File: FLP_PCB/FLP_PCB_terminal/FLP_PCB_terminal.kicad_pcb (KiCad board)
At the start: 2 copper layers, 84.1 x 84.1 mm, 79 parts, among them J1 SMA-J-P-X-ST-TH1, J2 OLED, Q1 Q_PMOS_DSG, U1 AMS1117-3.3, U2 STM32F103C8T6, U3 L86-M33, U4 MCP73831-2-OT, U5 CP2104, U6 TPS61200DRC, U7 USBLC6-2P6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

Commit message: PCB
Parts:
- Y2: footprint Crystal:Crystal_SMD_2012-2Pin_2.0x1.2mm -> Crystal:Crystal_SMD_2016-4Pin_2.0x1.6mm
- moved S2 178.8 mm to (49.0, 129.3)
- moved S1 178.8 mm to (49.0, 124.5)
- moved R3 168.1 mm to (71.5, 154.5)
- moved R4 149.6 mm to (71.5, 152.9)
- moved R8 148.1 mm to (94.7, 154.4)
- moved R16 146.3 mm to (94.7, 155.5)
- moved R9 146.1 mm to (94.7, 153.1)
- moved R17 145.9 mm to (94.7, 156.7)
- moved U7 140.1 mm to (111.0, 154.4), turned to 180 degrees
- moved C28 137.8 mm to (60.0, 134.3)
- moved R1 132.4 mm to (57.4, 123.7), turned to 180 degrees
- moved R2 132.1 mm to (57.4, 125.5), turned to 180 degrees
- moved C17 128.5 mm to (94.7, 149.4), turned to 180 degrees
- moved C18 125.3 mm to (94.7, 147.8)
- moved UART1 121.8 mm to (120.0, 154.2), turned to 90 degrees
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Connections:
- D1 pad A: (no net) -> 5v OUT
- D1 pad C: (no net) -> Net-(Charger1-VBUS)
- U2 pad 1: 3.3V OUT -> unconnected-(U2-VBAT-Pad1)
- U2 pad 18: PB0 -> unconnected-(U2-PB0-Pad18)
- Y2 pad 1: Net-(U8-XTB) -> (no net)
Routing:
- net Net-(BT1-+): track 0.00 -> 78.3 mm, vias 0 -> 2
- net 5v OUT: track 0.00 -> 74.0 mm, vias 0 -> 4
- net BOOT0: track 0.00 -> 70.7 mm, vias 0 -> 2
- net I2C SCL: track 0.00 -> 66.1 mm
- net I2C SDL: track 0.00 -> 54.2 mm, vias 0 -> 2
- net NRST: track 0.00 -> 48.7 mm, vias 0 -> 2
- net 3.3V OUT: track 116.4 -> 68.3 mm, vias 8 -> 29
- net Buzzer: track 0.00 -> 43.2 mm, vias 0 -> 6
- net Net-(Charger1-VBUS): track 0.00 -> 43.1 mm, vias 0 -> 2
- net Find_Host: track 0.00 -> 43.0 mm, vias 0 -> 2
- net ID: track 0.00 -> 40.0 mm, vias 0 -> 2
- net Net-(U5-REGIN): track 0.00 -> 36.0 mm, vias 0 -> 3
- net Net-(Q1-D): track 0.00 -> 34.6 mm, vias 0 -> 2
- net Net-(U6-UVLO): track 0.00 -> 29.3 mm, vias 0 -> 4
- net PC_OSC_IN: track 0.00 -> 28.3 mm
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- added copper zone on In1.Cu, net 3.3V OUT
- added copper zone on B.Cu, net GND
- added copper zone on F.Cu, net GND
- added copper zone on In2.Cu, net GND
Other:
- board size 84.1 x 84.1 mm -> 80 x 80 mm
- copper layers 2 -> 4

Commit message: PCB finish
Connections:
- UART1 pad A1_B12: (no net) -> GND
- UART1 pad B1_A12: (no net) -> GND
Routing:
- net GND: track 149.5 -> 157.4 mm, vias 58 -> 60
- net Net-(U5-REGIN): track 36.0 -> 38.2 mm

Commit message: code adding
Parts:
- BZ1: footprint Buzzer_Beeper:Buzzer_15x7.5RM7.6 -> Buzzer_Beeper:Buzzer_12x9.5RM7.6
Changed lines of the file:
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@@
 			(outputformat 1)
 			(mirror no)
-			(drillshape 1)
+			(drillshape 0)
 			(scaleselection 1)
 			(outputdirectory "")
@@
 		)
 	)
-	(footprint "Buzzer_Beeper:Buzzer_15x7.5RM7.6"
+	(footprint "Buzzer_Beeper:Buzzer_12x9.5RM7.6"
 		(layer "F.Cu")
 		(at 71.28 118.25)
-		(descr "Generic Buzzer, D15mm height 7.5mm with RM7.6mm")
+		(descr "Generic Buzzer, D12mm height 9.5mm with RM7.6mm")
 		(tags "buzzer")
 		(property "Reference" "BZ1"
-			(at 13.13 0.24 0)
+			(at 3.8 -7.2 0)
 			(layer "F.SilkS")
 			(effects
@@
 		)
 		(property "Value" "Buzzer"
-			(at 3.81 8.89 0)
+			(at 3.8 7.4 0)
 			(layer "F.Fab")
 			(effects
@@
 			)
 		)
-		(property "Description" "Buzzer, polarized"
+		(property "Description" ""
 			(at 0 0 0)
 			(unlocked yes)
@@
 		(fp_circle
 			(center 3.8 0)
-			(end 11.4 0)
+			(end 9.9 0)
 			(stroke
 				(width 0.12)
@@
 		(fp_circle
 			(center 3.8 0)
-			(end 11.55 0)
+			(end 10.05 0)
 			(stroke
 				(width 0.05)
@@
 		(fp_circle
 			(center 3.8 0)
-			(end 11.3 0)
+			(end 9.8 0)
 			(stroke
 				(width 0.1)
@@
 		)
 		(embedded_fonts no)
-		(model "${KICAD9_3DMODEL_DIR}/Buzzer_Beeper.3dshapes/Buzzer_15x7.5RM7.6.wrl"
+		(model "${KICAD9_3DMODEL_DIR}/Buzzer_Beeper.3dshapes/Buzzer_12x9.5RM7.6.wrl"
 			(offset
 				(xyz 0 0 0)

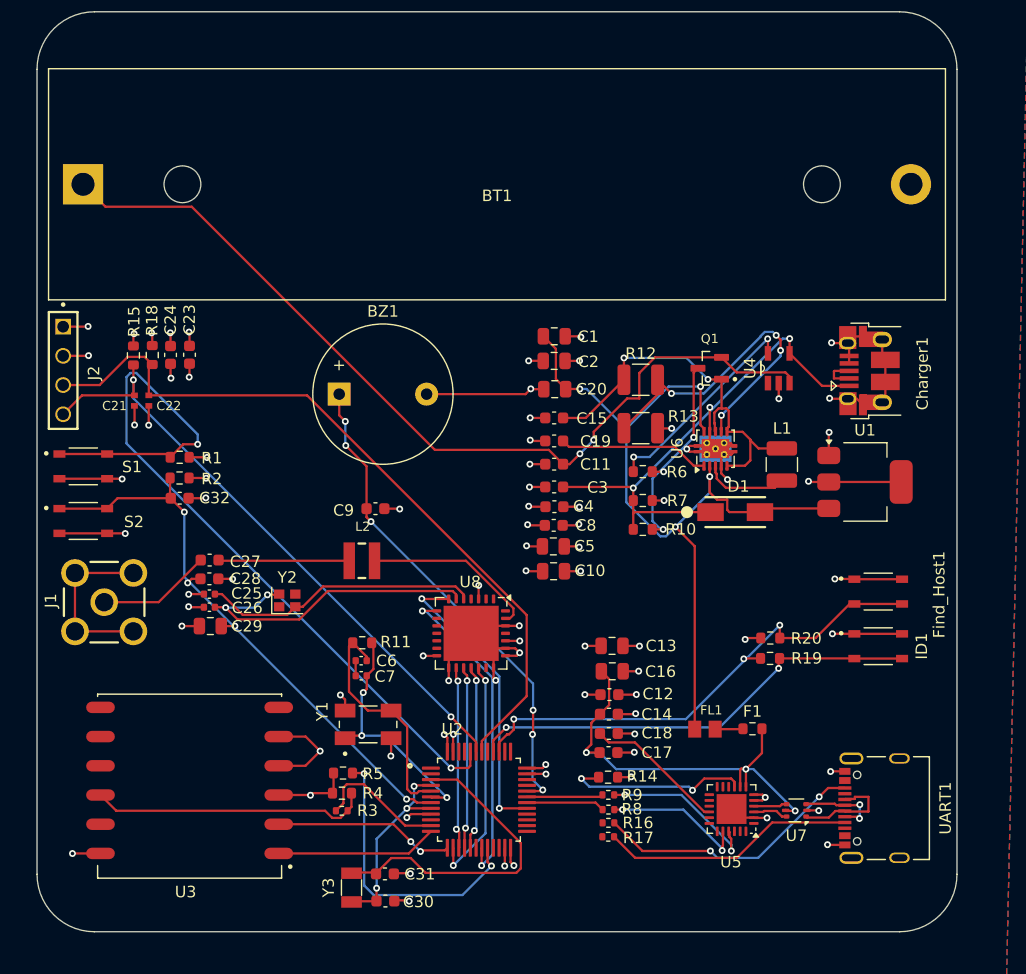
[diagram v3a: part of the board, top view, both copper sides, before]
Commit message: PCB build up -> nomal modify
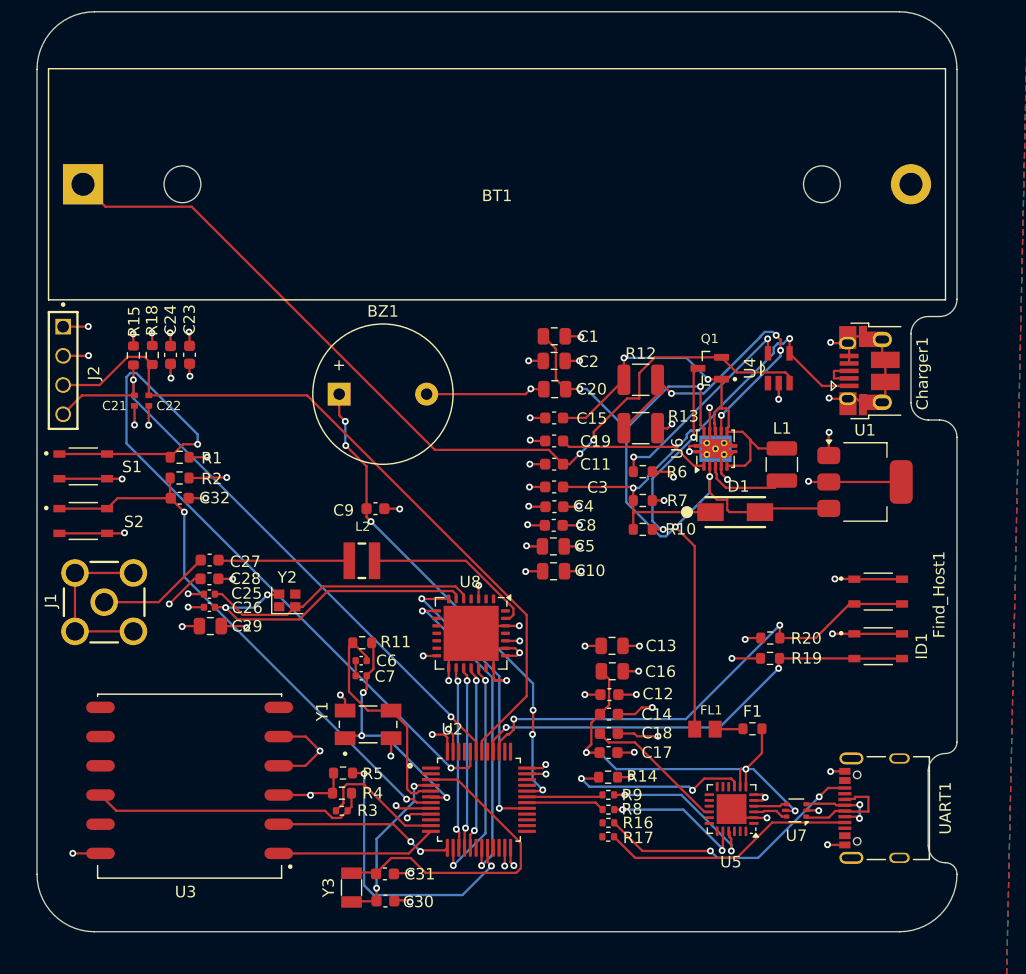
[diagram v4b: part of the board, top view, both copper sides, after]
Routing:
- net GND: track 157.4 -> 169.2 mm
- net 3.3V OUT: track 68.3 -> 72.2 mm
- net Net-(Charger1-VBUS): track 43.1 -> 43.8 mm
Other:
- outline, holes or cut-outs redrawn
